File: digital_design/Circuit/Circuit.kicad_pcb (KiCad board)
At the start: 2 copper layers, 100 x 56.1 mm, 36 parts, among them J1 RJ45, J2 RJ45, J3 Conn_01x03_Socket, J4 Conn_01x03_Socket, J5 BAT+, J6 BAT-, Q1 IRF540N, Q2 IRF9540N, U1 PC817, U2 PC817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

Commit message: Updated Design as per requirement
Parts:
- removed D5: LED_BGRK, Connector_PinSocket_2.54mm:PinSocket_1x04_P2.54mm_Vertical
- removed RV1: 500ohm, Potentiometer_THT:Potentiometer_Bourns_3296W_Vertical
- added D3: LED_BGKR, Connector_PinSocket_2.54mm:PinSocket_1x04_P2.54mm_Vertical, F.Cu at (127.9, 92.2)
- added R6: 180, Resistor_THT:R_Axial_DIN0207_L6.3mm_D2.5mm_P7.62mm_Horizontal, F.Cu at (114.5, 87.1)
- H1, H2, H3, H4: footprint MountingHole:MountingHole_5.3mm_M5_DIN965_Pad -> MountingHole:MountingHole_4mm
- J3, J4: value Conn_01x03_Socket -> 01x03
- J5, J6: footprint Connector_PinSocket_2.54mm:PinSocket_1x01_P2.54mm_Vertical -> MountingHole:MountingHole_3.2mm_M3_DIN965_Pad_TopBottom
- R11, R3: footprint Resistor_THT:R_Axial_DIN0207_L6.3mm_D2.5mm_P7.62mm_Horizontal -> Resistor_THT:R_Axial_DIN0207_L6.3mm_D2.5mm_P10.16mm_Horizontal
- moved H2 51.8 mm to (195.1, 102.2)
- moved H1 51.3 mm to (195.1, 78.2)
- moved J6 50.1 mm to (190.9, 59.7)
- moved Debug_pin1 49.9 mm to (143.8, 82.6)
- moved Bridge1 49.5 mm to (136.5, 62.3)
- moved J1 49.5 mm to (151.6, 88.4)
- moved J2 49.5 mm to (172.6, 88.4)
- moved J4 49.5 mm to (122.8, 94.1)
- moved R10 49.5 mm to (117.9, 79.5)
- moved R8 49.5 mm to (143.8, 71.8)
- moved U3 49.5 mm to (135.2, 57.9)
- moved C1 49.5 mm to (128.2, 79.1)
- moved J3 49.5 mm to (115.5, 97.4)
- moved R11 49.5 mm to (129.6, 75.9)
- moved R12 49.5 mm to (129.6, 72.9)
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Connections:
- J3 pad 1: IN_OUT- -> unconnected-(J3-Pin_1-Pad1)
- J3 pad 2: unconnected-(J3-Pin_2-Pad2) -> IN_OUT+
- J4 pad 1: unconnected-(J4-Pin_1-Pad1) -> BAT_OUT+
- J4 pad 3: IN_OUT+ -> IN_OUT-
- Q2 pad 3: IN_OUT+ -> BAT_OUT+
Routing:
- net BAT_OUT+: track 0.00 -> 88.4 mm
- net Net-(D3-RA): track 1.83 -> 75.4 mm
- net Net-(D3-GA): track 2.53 -> 66.2 mm
- net Net-(D3-BA): track 3.14 -> 55.4 mm
- net IN_OUT-: track 120.0 -> 151.4 mm
- net BAT-: track 261.8 -> 285.8 mm
- net IN_OUT+: track 104.4 -> 90.8 mm
- net BAT+: track 103.0 -> 114.6 mm
- net not NMOS_CONTROL: track 29.5 -> 22.4 mm
- net V_bat_adc: track 16.9 -> 10.3 mm
- net +5V: track 32.2 -> 28.5 mm
- net Net-(Debug_pin1-Pin_2): track 3.27 -> 5.13 mm
- net Net-(Debug_pin1-Pin_3): track 3.27 -> 5.13 mm
- net PMOS_CONTROL: track 31.6 -> 30.3 mm
- net Net-(R3-Pad1): track 3.26 -> 4.36 mm
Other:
- board size 100 x 56.1 mm -> 100 x 54.5 mm

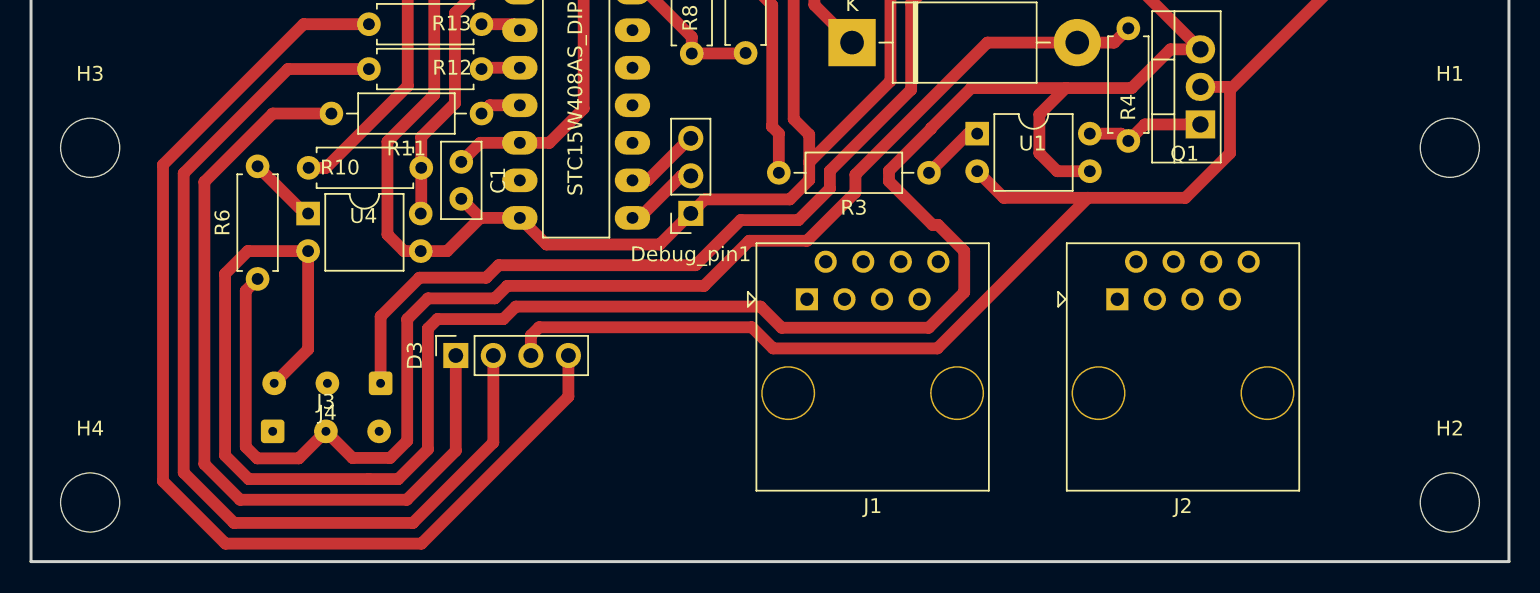
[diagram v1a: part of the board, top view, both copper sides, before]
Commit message: changed holes footprint
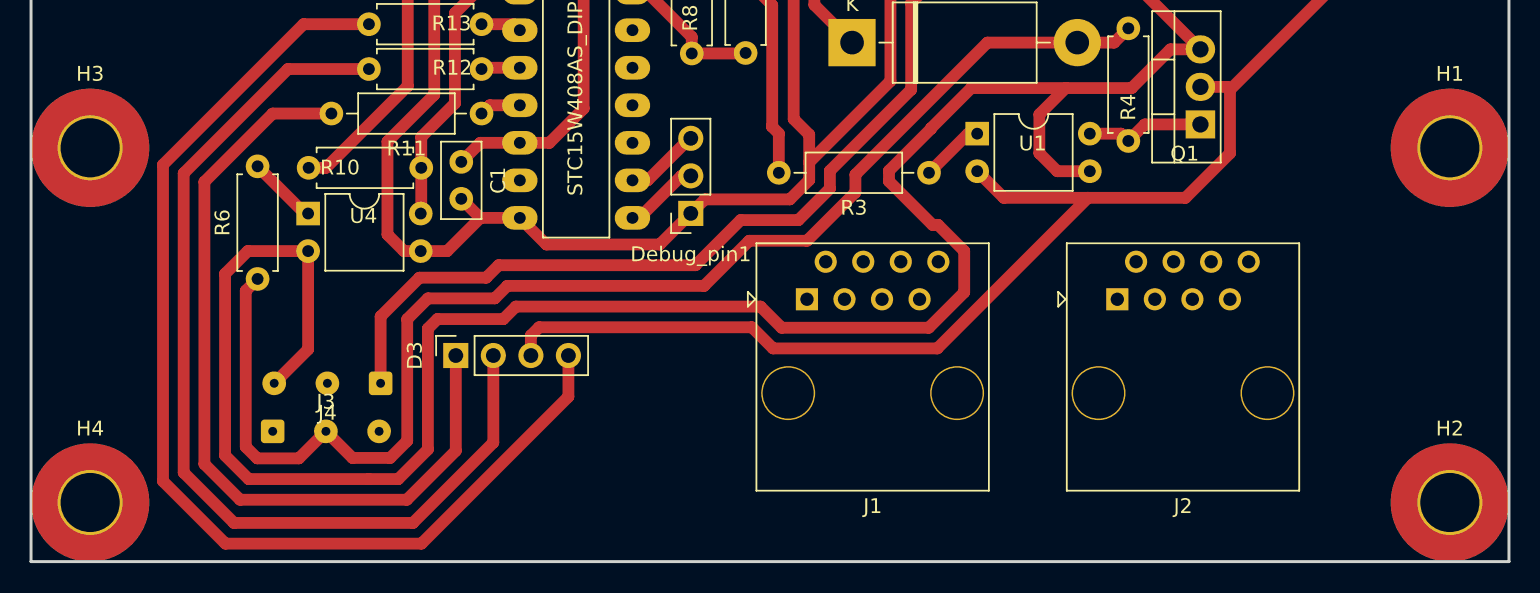
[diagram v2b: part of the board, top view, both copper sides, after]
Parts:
- H1, H2, H3, H4: footprint MountingHole:MountingHole_4mm -> MountingHole:MountingHole_4mm_Pad_TopBottom
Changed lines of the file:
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@@
     )
   )
-  (footprint "MountingHole:MountingHole_4mm" (layer "F.Cu")
+  (footprint "MountingHole:MountingHole_4mm_Pad_TopBottom" (layer "F.Cu")
     (at 103.138 102.1928)
-    (descr "Mounting Hole 4mm, no annular")
-    (tags "mounting hole 4mm no annular")
+    (descr "Mounting Hole 4mm")
+    (tags "mounting hole 4mm")
     (property "Sheetfile" "Circuit.kicad_sch")
     (property "Sheetname" "")
@@
     (fp_circle (center 0 0) (end 4.25 0)
       (stroke (width 0.05) (type solid)) (fill none) (layer "F.CrtYd"))
-    (pad "" np_thru_hole circle (at 0 0) (size 4 4) (drill 4) (layers "*.Cu" "*.Mask"))
+    (pad "1" thru_hole circle (at 0 0) (size 4.4 4.4) (drill 4) (layers "*.Cu" "*.Mask"))
+    (pad "1" connect circle (at 0 0) (size 8 8) (layers "F.Cu" "F.Mask"))
+    (pad "1" connect circle (at 0 0) (size 8 8) (layers "B.Cu" "B.Mask"))
   )
   (footprint "Package_DIP:DIP-4_W7.62mm" (layer "F.Cu")
@@
     )
   )
-  (footprint "MountingHole:MountingHole_4mm" (layer "F.Cu")
+  (footprint "MountingHole:MountingHole_4mm_Pad_TopBottom" (layer "F.Cu")
     (at 103.138 78.1928)
-    (descr "Mounting Hole 4mm, no annular")
-    (tags "mounting hole 4mm no annular")
+    (descr "Mounting Hole 4mm")
+    (tags "mounting hole 4mm")
     (property "Sheetfile" "Circuit.kicad_sch")
     (property "Sheetname" "")
@@
     (fp_circle (center 0 0) (end 4.25 0)
       (stroke (width 0.05) (type solid)) (fill none) (layer "F.CrtYd"))
-    (pad "" np_thru_hole circle (at 0 0) (size 4 4) (drill 4) (layers "*.Cu" "*.Mask"))
+    (pad "1" thru_hole circle (at 0 0) (size 4.4 4.4) (drill 4) (layers "*.Cu" "*.Mask"))
+    (pad "1" connect circle (at 0 0) (size 8 8) (layers "F.Cu" "F.Mask"))
+    (pad "1" connect circle (at 0 0) (size 8 8) (layers "B.Cu" "B.Mask"))
   )
   (footprint "Connector_PinSocket_2.54mm:PinSocket_1x03_P2.54mm_Vertical" (layer "F.Cu")
@@
     )
   )
-  (footprint "MountingHole:MountingHole_4mm" (layer "F.Cu")
+  (footprint "MountingHole:MountingHole_4mm_Pad_TopBottom" (layer "F.Cu")
     (at 195.138 78.1928)
-    (descr "Mounting Hole 4mm, no annular")
-    (tags "mounting hole 4mm no annular")
+    (descr "Mounting Hole 4mm")
+    (tags "mounting hole 4mm")
     (property "Sheetfile" "Circuit.kicad_sch")
     (property "Sheetname" "")
@@
     (fp_circle (center 0 0) (end 4.25 0)
       (stroke (width 0.05) (type solid)) (fill none) (layer "F.CrtYd"))
-    (pad "" np_thru_hole circle (at 0 0) (size 4 4) (drill 4) (layers "*.Cu" "*.Mask"))
-  )
-  (footprint "MountingHole:MountingHole_4mm" (layer "F.Cu")
+    (pad "1" thru_hole circle (at 0 0) (size 4.4 4.4) (drill 4) (layers "*.Cu" "*.Mask"))
+    (pad "1" connect circle (at 0 0) (size 8 8) (layers "F.Cu" "F.Mask"))
+    (pad "1" connect circle (at 0 0) (size 8 8) (layers "B.Cu" "B.Mask"))
+  )
+  (footprint "MountingHole:MountingHole_4mm_Pad_TopBottom" (layer "F.Cu")
     (at 195.138 102.1928)
-    (descr "Mounting Hole 4mm, no annular")
-    (tags "mounting hole 4mm no annular")
+    (descr "Mounting Hole 4mm")
+    (tags "mounting hole 4mm")
     (property "Sheetfile" "Circuit.kicad_sch")
     (property "Sheetname" "")
@@
     (fp_circle (center 0 0) (end 4.25 0)
       (stroke (width 0.05) (type solid)) (fill none) (layer "F.CrtYd"))
-    (pad "" np_thru_hole circle (at 0 0) (size 4 4) (drill 4) (layers "*.Cu" "*.Mask"))
+    (pad "1" thru_hole circle (at 0 0) (size 4.4 4.4) (drill 4) (layers "*.Cu" "*.Mask"))
+    (pad "1" connect circle (at 0 0) (size 8 8) (layers "F.Cu" "F.Mask"))
+    (pad "1" connect circle (at 0 0) (size 8 8) (layers "B.Cu" "B.Mask"))
   )
   (footprint "Resistor_THT:R_Axial_DIN0207_L6.3mm_D2.5mm_P7.62mm_Horizontal" (layer "F.Cu")

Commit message: minor changes
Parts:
- R6: value 180 -> 1k
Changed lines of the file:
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@@
     (property "ki_keywords" "R res resistor")
     (attr through_hole)
-    (fp_text reference "R6" (at 3.81 -2.37 90) (layer "F.SilkS")
+    (fp_text reference "R6" (at 1.9414 -0.0418 90) (layer "F.SilkS")
         (effects (font (size 1 1) (thickness 0.15)))
     )
-    (fp_text value "180" (at 3.81 2.37 90) (layer "F.Fab")
+    (fp_text value "1k" (at 5.2664 0.0082 90) (layer "F.Fab")
         (effects (font (size 1 1) (thickness 0.15)))
     )
-    (fp_text user "${REFERENCE}" (at 3.81 0 90) (layer "F.Fab")
+    (fp_text user "${REFERENCE}" (at 1.9414 -0.0418 90) (layer "F.Fab")
         (effects (font (size 1 1) (thickness 0.15)))
     )
